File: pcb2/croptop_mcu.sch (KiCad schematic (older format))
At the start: 44 parts

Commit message: Added USB port control
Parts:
- removed C?: 0.1uF, Capacitor_SMD:C_0402_1005Metric, symbol Device:C
- removed C? (x3): 10uF, Capacitor_SMD:C_0805_2012Metric, symbol Device:C
- removed C? (x2): 26pF, Capacitor_SMD:C_0402_1005Metric, symbol Device:C
- removed J?: USB_A, croptop:USB_A_Assmann_Horizontal, symbol Connector:USB_A
- removed L?: 10uH, Inductor_SMD:L_1210_3225Metric, symbol Device:L
- removed R? (x2): 0, Resistor_SMD:R_0402_1005Metric, symbol Device:R
- removed R? (x2): 2K, Resistor_SMD:R_0402_1005Metric, symbol Device:R
- removed R?: 10, Resistor_SMD:R_0402_1005Metric, symbol Device:R
- removed U?: PIC32MX795F512L, Package_QFP:TQFP-100_12x12mm_P0.4mm, symbol CropTop:PIC32MX795F512L
- removed U? (x2): PUSBM5V5X4, croptop:PUSBM5V5X4, symbol CropTop:PUSBM5V5X4
- removed Y?: CXO, croptop:ABLS_OX, symbol Device:Crystal
- added C? (x2): 0.1uF, Capacitor_SMD:C_0402_1005Metric, symbol Device:C
- added C? (x2): 10uF, Capacitor_SMD:C_0402_1005Metric, symbol Device:C
- added D? (x2): LED, LED_SMD:LED_0805_2012Metric, symbol Device:LED
- added F?: Polyfuse, symbol Device:Polyfuse
- added J?: USB_A, croptop:USB_A_Assmann_Horizontal, symbol Connector:USB_A
- added R? (x4): R, symbol Device:R
- added SW?: SW_Push, symbol Switch:SW_Push
- added TP? (x8): TestPoint, symbol Connector:TestPoint
- added U?: TPD4E1U06, symbol CropTop:TPD4E1U06
- added U? (x2): TPS22915, symbol CropTop:TPS22915
- added U?: FSUSB42, symbol CropTop:FSUSB42
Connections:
- net labels added: ADC_MISO, CONFIG_ADC, DC_FAULT, DC_PWM_1, DC_PWM_2, PMOD_PWM_1, PMOD_PWM_2, USB_EN, USB_PWR_1, USB_PWR_2, USB_SEL
- net labels removed: ADC_1, ADC_2, ADC_3, ADC_4, ADC_5, ADC_6, BTN_A, BTN_B, DRV_FAULT, DRV_FLT, DRV_IN1, DRV_IN2, DRV_PWM1, DRV_PWM2, DRV_PWM_1, DRV_PWM_2, LED_A, LED_B, LIN_VOLT, MISO, MOSI, NAND_HOLD, NAND_WP, ROTARY_1A, ROTARY_1B, ROT_Y1, ROT_Y2, RX, SCL, SCLK, SCLK2, SDA, SDIO2, SDO2, SS2, TX
- wire segments 230 -> 193
- no-connect marks 61 -> 8
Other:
- note added: "MCU Reset"
- note added: "PICKit3 Programming Header"
- note added: "Software Config Divider"
- note removed: "Address = 0101100b"
- note removed: "PICKit3 Header"
- moved on the sheet: C?, FID?, H?, J?, L?, R?, U?A, U?B, Y?

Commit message: Added important notes
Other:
- note added: "accomplash"
- note added: "and"
- note added: "control alt delete muthafucka"
- note added: "hmmmm no"
- note added: "j? k? l? mnop?"
- note added: "squablo"
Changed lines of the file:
@@
 Wire Wire Line
 	3500 4750 3750 4750
+Text Notes 4000 3150 0    50   ~ 0
+control alt delete muthafucka
+Text Notes 5500 2150 0    50   ~ 10
+hmmmm no
+Text Notes 6000 3050 3    50   Italic 10
+squablo
+Text Notes 6100 3150 3    50   Italic 10
+and
+Text Notes 6200 2950 3    50   Italic 10
+accomplash
+Text Notes 3750 1600 3    50   Italic 10
+j? k? l? mnop?
 $EndSCHEMATC

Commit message: Schematic near completion
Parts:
- removed C?: 0.1uF, Capacitor_SMD:C_0402_1005Metric, symbol Device:C
- removed C?: 10uF, Capacitor_SMD:C_0402_1005Metric, symbol Device:C
- removed D?: LED, LED_SMD:LED_0805_2012Metric, symbol Device:LED
- removed F?: Polyfuse, symbol Device:Polyfuse
- removed R?: R, symbol Device:R
- removed TP? (x3): TestPoint, symbol Connector:TestPoint
- removed U? (x2): TPS22915, symbol CropTop:TPS22915
- added C?: 0.1uF, Capacitor_SMD:C_0402_1005Metric, symbol Device:C
- added C?: 10uF, Capacitor_SMD:C_0402_1005Metric, symbol Device:C
- added D?: LED, LED_SMD:LED_0805_2012Metric, symbol Device:LED
- added R? (x7): 10k, Resistor_SMD:R_0402_1005Metric, symbol Device:R
- added R?: 220, Resistor_SMD:R_0402_1005Metric, symbol Device:R
- added TP? (x5): TestPoint, symbol Connector:TestPoint
- added U? (x2): AP22802AW5, symbol CropTop:AP22802AW5
- added U?: 74AUP2G57, symbol CropTop:74AUP2G57
- C?: footprint Capacitor_SMD:C_0805_2012Metric -> Capacitor_SMD:C_0402_1005Metric
- C?: footprint (none) -> Capacitor_SMD:C_0402_1005Metric
- FID? (x2): value FIDUCIAL -> Fiducial
- H?: value Top Left -> 4mm Mounting Hole
- H?: value Top Right -> 4mm Mounting Hole
- H?: value Bottom Left -> 4mm Mounting Hole
- H?: value Bottom Right -> 4mm Mounting Hole
- J?: value 5V USB -> 10118193-0001LF
- J? (x2): value USB_A -> USB-A1HSW6; Note (none) -> USB A
- J?: value PICKit3 Header -> 68000-206HLF
- L?: footprint (none) -> Inductor_SMD:L_1210_3225Metric
- R? (x2): value R -> 10k; footprint (none) -> Resistor_SMD:R_0402_1005Metric
- R?: value R -> 220; footprint (none) -> Resistor_SMD:R_0402_1005Metric
- U? (x2): value PIC32MX795F512L-80I_PT_0 -> PIC32MX795F512L; Category Integrated Circuits (ICs) -> (none); DK_Datasheet_Link http://www.microchip.com/mymicrochip/filehandler.aspx?ddocn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 -> (none); DK_Detail_Page /product-detail/en/microchip-technology/PIC32MX795F512L-80I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 -> (none); Description IC MCU 32BIT 512KB FLASH 100TQFP -> (none); Digi-Key_PN PIC32MX795F512L-80I/PT-ND -> (none); Family Embedded - Microcontrollers -> (none); MPN PIC32MX795F512L-80I/PT -> (none); Manufacturer Microchip Technology -> (none); Status Active -> (none)
- Y?: value CXO -> ABLS-8.000MHZ-B4-T
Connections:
- net labels added: USB_FLG_1, USB_FLG_2, ~USB_EN
- net labels removed: USB_EN, USB_PWR_1, USB_PWR_2
- wire segments 193 -> 246
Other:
- note added: "(74AUP2G57 Truth Table)"
- note added: "(Configuration)"
- note added: "Cart: 10K\nPusher: 10K\nStabber: 2K"
- note added: "Cart: 2K\nPusher: 10K\nStabber: 10K"
- note removed: "accomplash"
- note removed: "and"
- note removed: "control alt delete muthafucka"
- note removed: "hmmmm no"
- note removed: "j? k? l? mnop?"
- note removed: "squablo"
- moved on the sheet: C?, J?, L?, R?, U?A, U?B, Y?

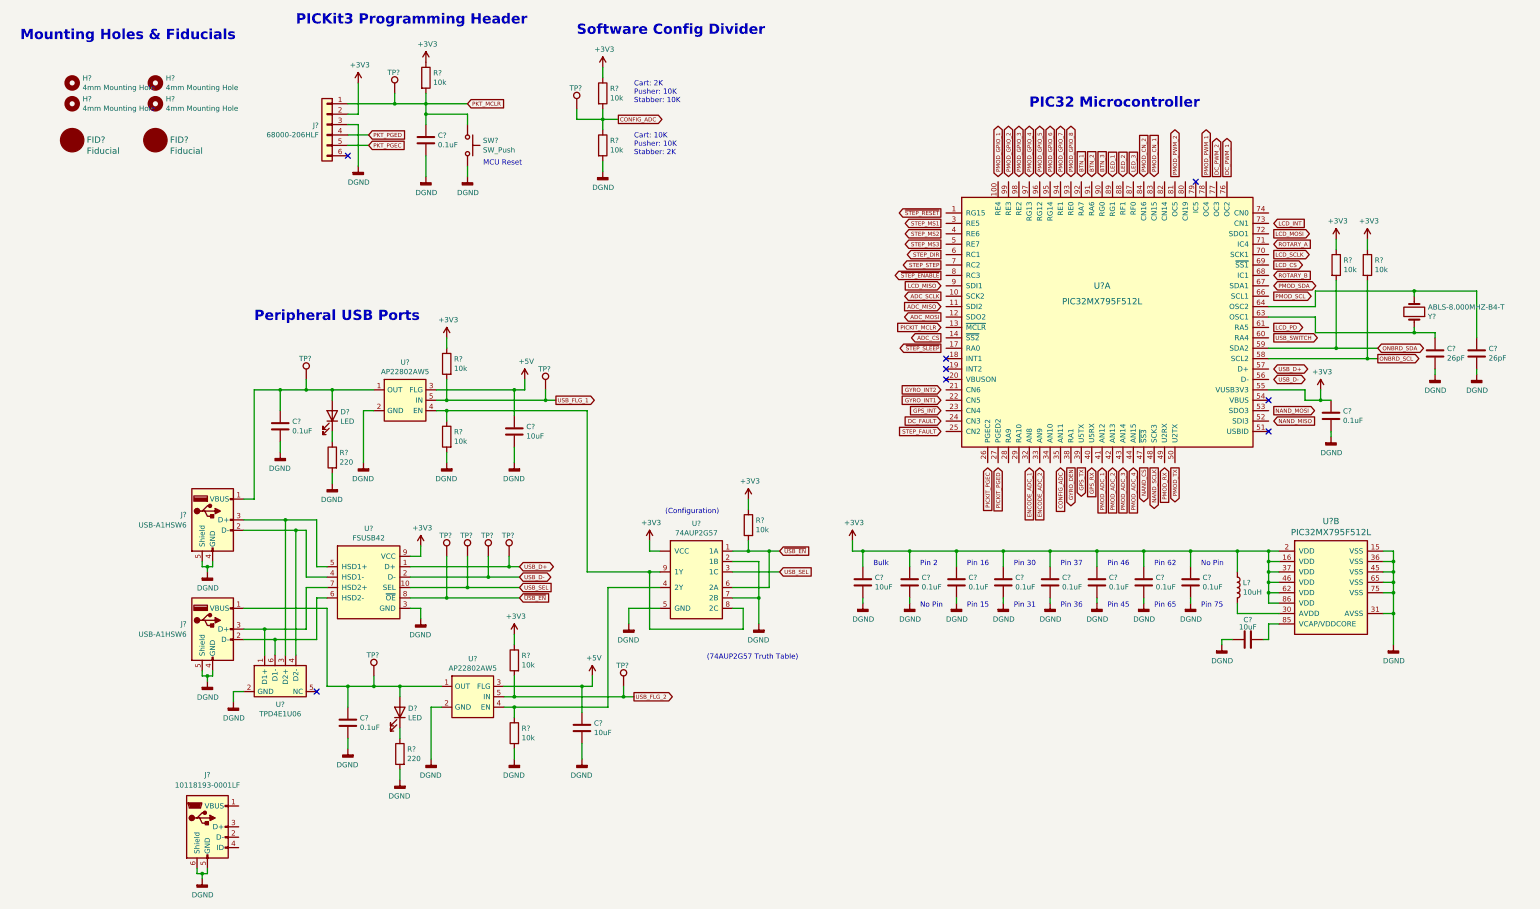
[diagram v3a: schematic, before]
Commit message: Added pmod
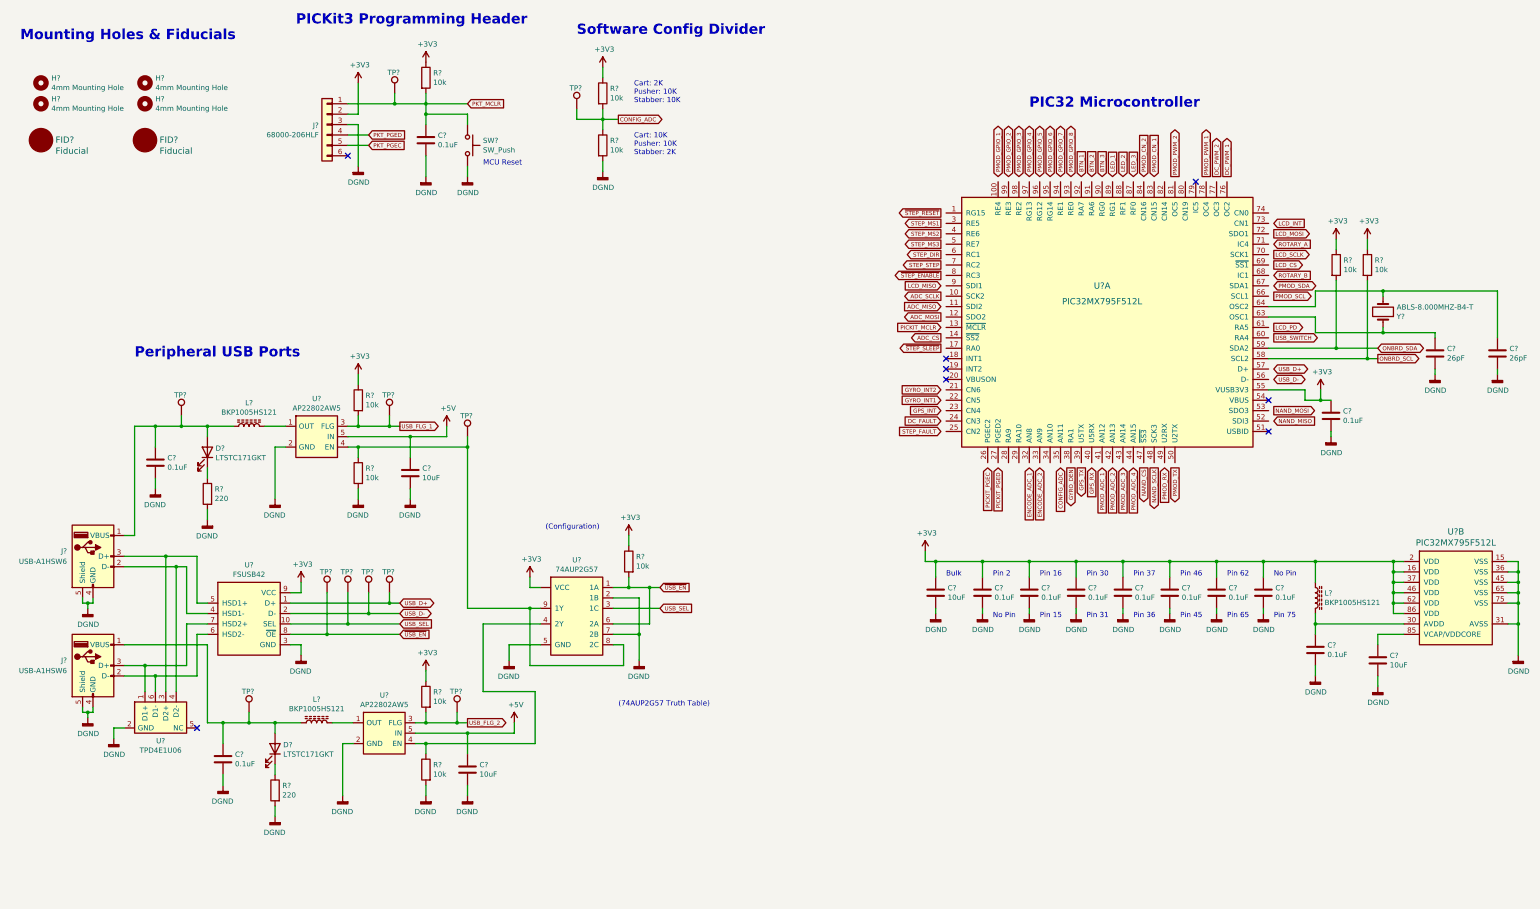
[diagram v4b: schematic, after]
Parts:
- removed C?: 10uF, Capacitor_SMD:C_0402_1005Metric, symbol Device:C
- removed J?: 10118193-0001LF, croptop:USB_Micro-B_Molex_47346-0001, symbol Connector:USB_B_Micro
- removed L?: 10uH, Inductor_SMD:L_1210_3225Metric, symbol Device:L
- removed R? (x2): 10k, Resistor_SMD:R_0402_1005Metric, symbol Device:R
- removed U?: AP22802AW5, symbol CropTop:AP22802AW5
- added C?: 0.1uF, Capacitor_SMD:C_0402_1005Metric, symbol Device:C
- added C?: 10uF, Capacitor_SMD:C_0402_1005Metric, symbol Device:C
- added L? (x3): BKP1005HS121, symbol Device:L_Core_Ferrite
- added R? (x2): 10k, Resistor_SMD:R_0402_1005Metric, symbol Device:R
- added TP?: TestPoint, symbol Connector:TestPoint
- added U?: AP22802AW5, symbol CropTop:AP22802AW5
- D? (x2): value LED -> LTSTC171GKT
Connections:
- net +3V3: now also L?.1, R?.1
- net +5V: now also U?.5 (IN), C?.1, U?.5 (IN); no longer U?.3 (FLG)
- net DGND: now also C?.2, C?.2, C?.2, R?.2, U?.2 (GND); no longer C?.1
- net USB_FLG_1: now also U?.3 (FLG), TP?.1; no longer TP?.1, U?.5 (IN)
- net USB_FLG_2: now also R?.2, U?.3 (FLG)
- net at C?.1, D?.2 (A), J?.1 (VBUS)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: now also L?.1; no longer U?.1 (OUT)
- net at R?.1, U?.4 (EN), U?.8 (2C)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: now also TP?.1
- net at C?.1, D?.2 (A), J?.1 (VBUS)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: now also L?.1
- net at U?.4 (2Y): now also R?.1, U?.4 (EN)
- net at U?.30 (AVDD): now also C?.1, L?.2
- net at U?.85 (VCAP/VDDCORE): now also C?.1; no longer C?.2
- new net: L?.2, U?.1 (OUT) (x2)
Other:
- moved on the sheet: C?, D?, FID?, H?, J?, R?, TP?, U?, U?B, Y?

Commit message: pwm
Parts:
- R1, R2: renamed from R?; value 220 -> 220Ω
- R10, R11, R12, R3, R4, R5, R6, R7, R8, R9: renamed from R?; value 10k -> 10kΩ
- gave numbers to parts that had none: 51
